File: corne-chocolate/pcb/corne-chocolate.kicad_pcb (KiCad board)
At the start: 2 copper layers, 133.8 x 91.4 mm, 109 parts, among them J2 nice!view, J3 Battery, J4 Battery, SW1 1U, SW10 1U, SW11 1U, SW12 1U, SW13 1U, SW14 1U, SW15 1U, SW16 1U, SW17 1U, SW18 1U, SW19 1U, SW2 1U, SW20 1U, SW21 1.5U, SW22 SW_PUSH, SW23 SW_SPDT, SW3 1U, SW4 1U, SW5 1U, SW6 1U, SW7 1U, SW8 1U, SW9 1U, U1 ProMicro

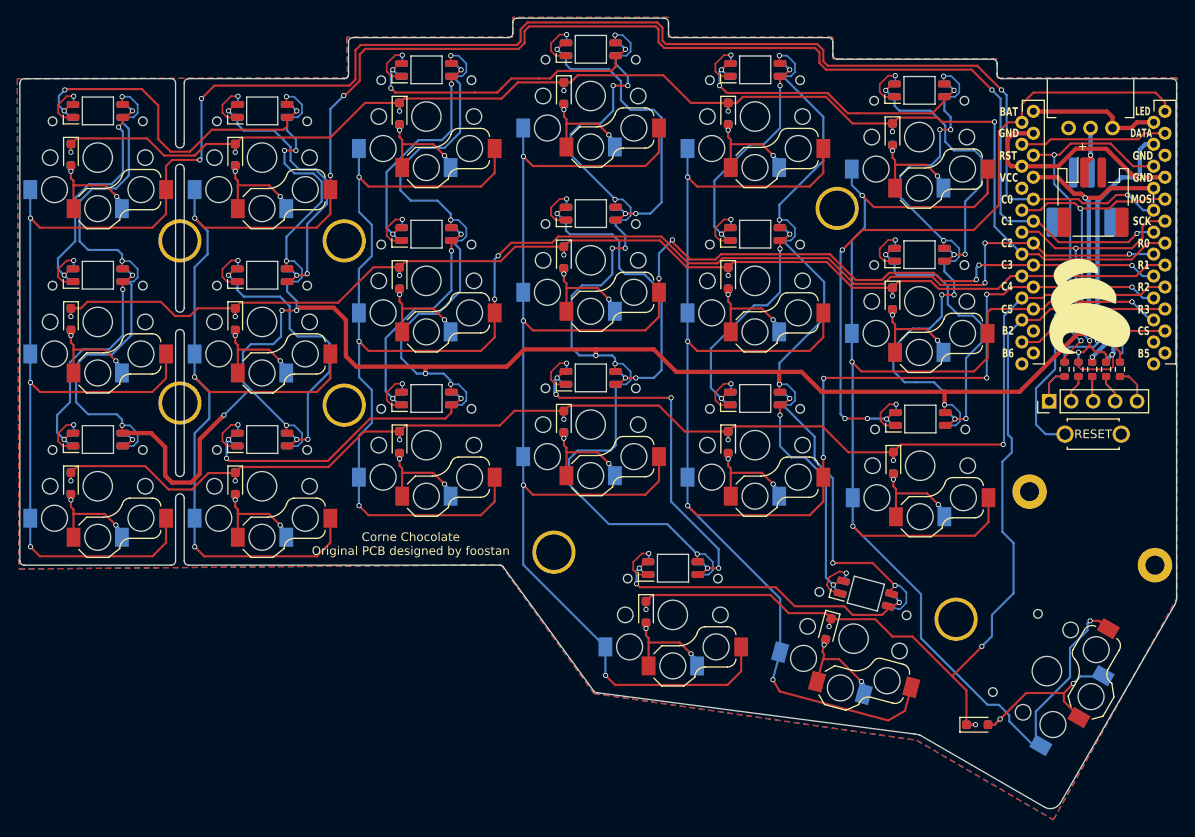
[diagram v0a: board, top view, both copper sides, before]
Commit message: pcb remove per-switch LEDs
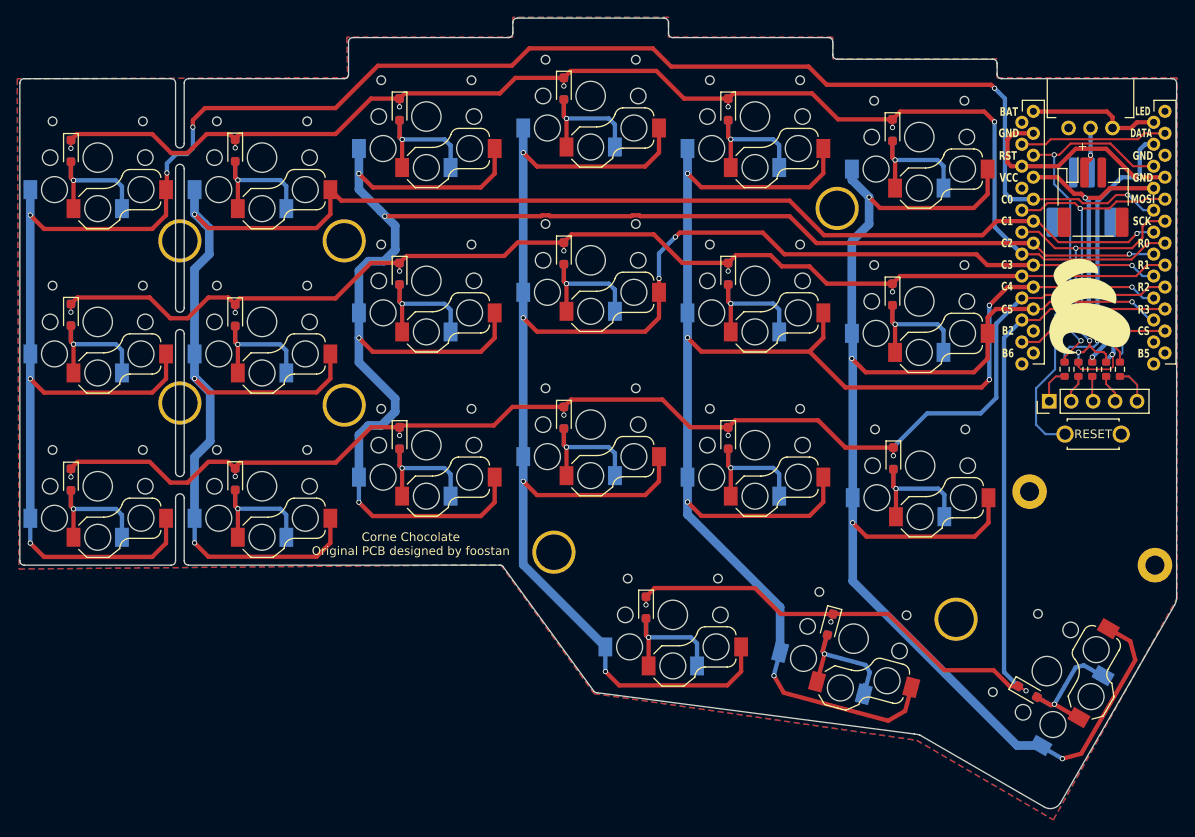
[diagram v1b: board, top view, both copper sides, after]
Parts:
- removed LED1, LED10, LED11, LED12, LED13, LED14, LED15, LED16, LED17, LED18, LED19, LED2, LED20, LED3, LED4, LED5, LED6, LED7, LED8, LED9: SK6812, corne-chocolate:SK6812MINI-E_doublesided
- moved D11 6.96 mm to (177.5, 138.9), turned to -30 degrees
- moved D21 6.96 mm to (177.5, 138.9), turned to -30 degrees
- moved D10 0.57 mm to (154.7, 131.1)
- moved D6 0.57 mm to (154.7, 131.1)
- moved D4 0.53 mm to (133.4, 129.2)
- moved D5 0.53 mm to (133.4, 129.2)
- moved D3 0.52 mm to (123.9, 69.2)
- moved D47 0.52 mm to (162.0, 111.9)
- moved D48 0.52 mm to (162.0, 111.9)
- moved D9 0.52 mm to (123.9, 69.2)
- moved D14 0.50 mm to (85.9, 114.3)
- moved D22 0.50 mm to (85.9, 76.3)
- moved D23 0.50 mm to (85.9, 76.3)
- moved D24 0.50 mm to (66.9, 95.3)
- moved D25 0.50 mm to (66.9, 95.3)
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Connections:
- U1 pad 1: LED -> unconnected-(U1-TX0/PD3-Pad1)
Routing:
- net VCC: track 648.0 -> 36.4 mm, vias 39 -> 2
- net GND: track 185.5 -> 63.6 mm, vias 22 -> 2
- net LED: track 80.0 -> 0.00 mm, vias 4 -> 0
- net /L9: track 44.7 -> 0.00 mm, vias 5 -> 0
- net /L18: track 42.1 -> 0.00 mm, vias 3 -> 0
- net /L8: track 38.9 -> 0.00 mm, vias 3 -> 0
- net /L15: track 37.4 -> 0.00 mm, vias 3 -> 0
- net /L12: track 36.7 -> 0.00 mm, vias 3 -> 0
- net /L10: track 36.5 -> 0.00 mm, vias 3 -> 0
- net /L11: track 36.2 -> 0.00 mm, vias 3 -> 0
- net /L4: track 36.2 -> 0.00 mm, vias 3 -> 0
- net /L16: track 35.0 -> 0.00 mm, vias 3 -> 0
- net /L2: track 33.9 -> 0.00 mm, vias 3 -> 0
- net /L3: track 33.8 -> 0.00 mm, vias 3 -> 0
- net /L17: track 33.6 -> 0.00 mm, vias 3 -> 0
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
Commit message: pcb clean up mounting holes
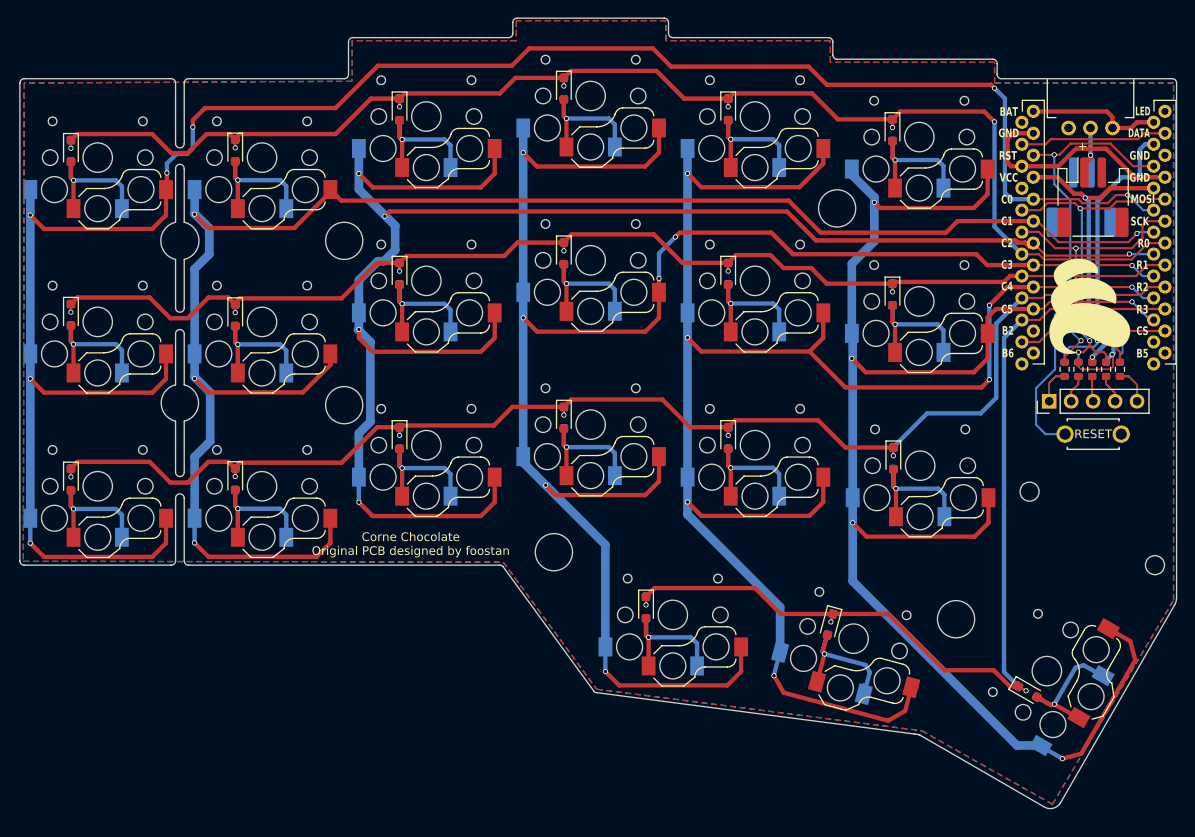
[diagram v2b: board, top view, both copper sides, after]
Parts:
- removed ? (x9): , kbd:LEGO_HOLE
- added H1: MountingHole, MountingHole:MountingHole_2.2mm_M2, F.Cu at (177.8, 115.8)
- added H2: MountingHole, MountingHole:MountingHole_2.2mm_M2, F.Cu at (192.2, 124.2)
- added H3: MountingHole, MountingHole:MountingHole_4.3mm_M4, F.Cu at (155.5, 83.0)
- added H4: MountingHole, MountingHole:MountingHole_4.3mm_M4, F.Cu at (98.5, 86.8)
- added H5: MountingHole, MountingHole:MountingHole_4.3mm_M4, F.Cu at (98.5, 105.8)
- added H6: MountingHole, MountingHole:MountingHole_4.3mm_M4, F.Cu at (169.2, 130.5)
- added H7: MountingHole, MountingHole:MountingHole_4.3mm_M4, F.Cu at (122.8, 122.8)
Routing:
- net col3: track 211.2 -> 208.4 mm
- net col1: track 203.0 -> 200.3 mm
- net col2: track 200.5 -> 198.4 mm
- net col4: track 197.0 -> 196.3 mm
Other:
- outline, holes or cut-outs redrawn
